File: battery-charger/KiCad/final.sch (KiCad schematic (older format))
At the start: 19 parts, among them Q1 MOSFET_P, SW1 SPST, U1 BQ2057W

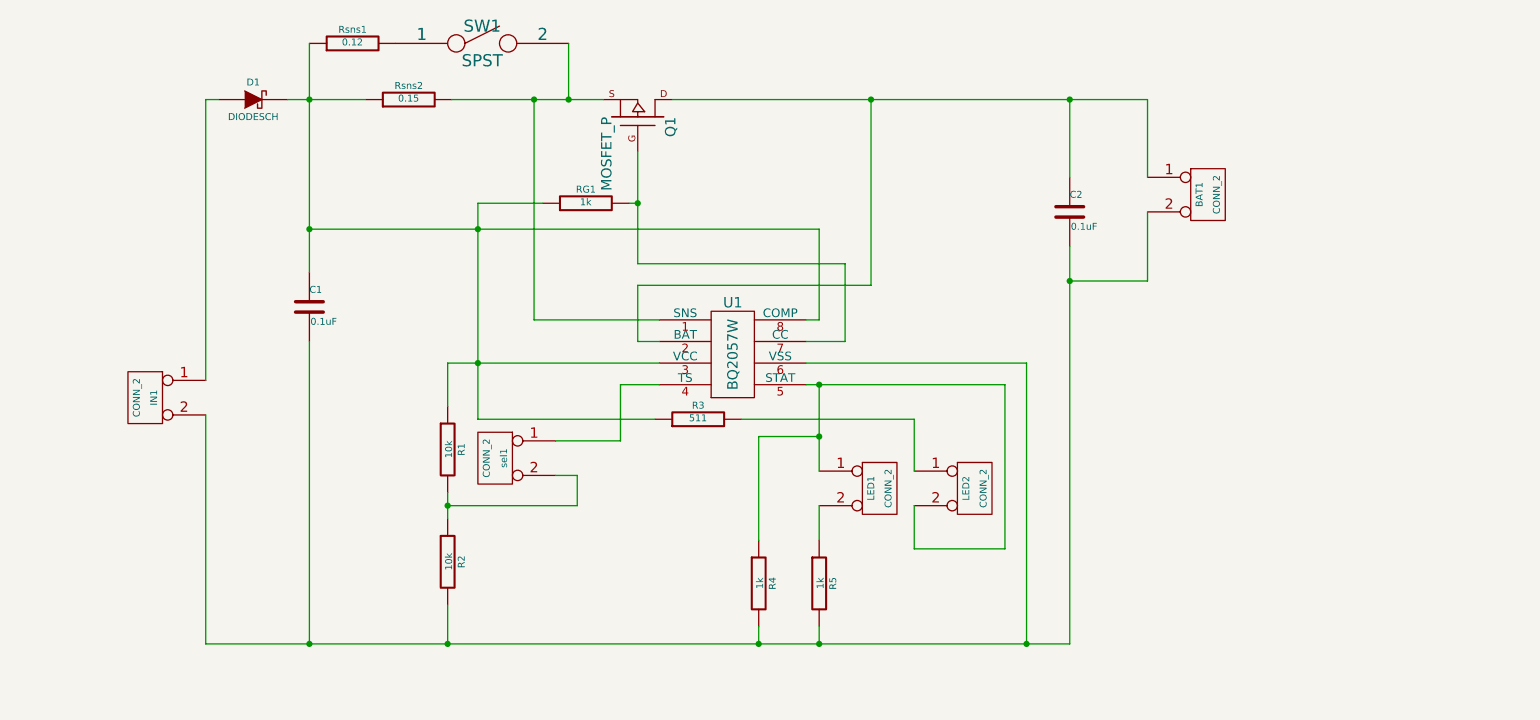
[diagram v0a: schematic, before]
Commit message: Link correctly the specific footprint library and change one component
The two connectors are repleaced by a 3-pin connector in order to reduce
length of power traces.
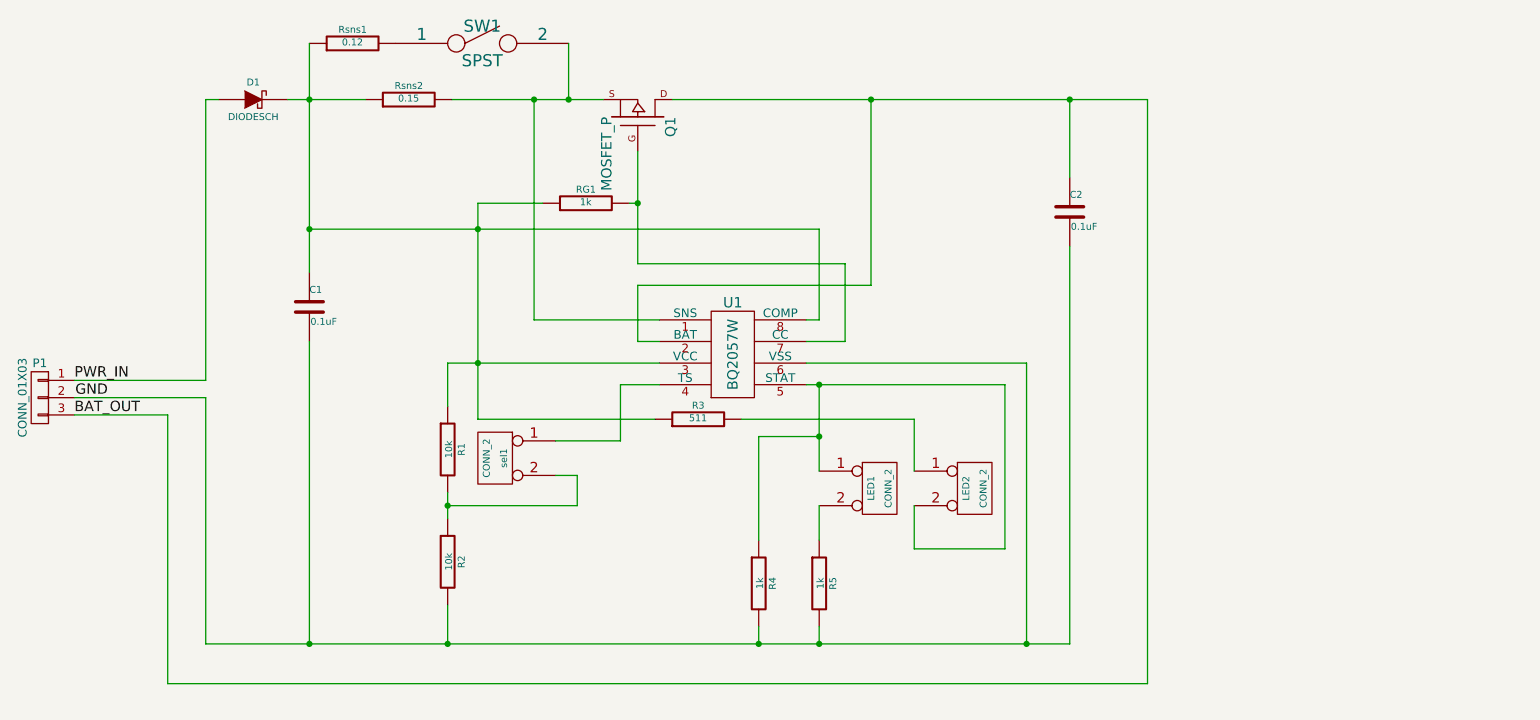
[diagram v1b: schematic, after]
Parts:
- removed BAT1, IN1: CONN_2, symbol CONN_2
- added P1: CONN_01X03, symbol CONN_01X03
- U1: footprint ~ -> (none)
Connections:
- net BAT_OUT: now reaches C2.1, Q1.D, U1.2 (BAT)
- net BAT_OUT: now also P1.3 (P3)
- net GND: now reaches C1.2, C2.2, R2.2, R4.2, R5.2, U1.6 (VSS)
- net GND: now also P1.2 (P2)
- net PWR_IN: now reaches D1.1 (A)
- net PWR_IN: now also P1.1 (P1)
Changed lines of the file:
@@
 EESchema Schematic File Version 2
-LIBS:final-rescue
 LIBS:power
 LIBS:device
@@
 LIBS:contrib
 LIBS:valves
+LIBS:special
 LIBS:final-cache
 EELAYER 25 0
@@
 	1    0    0    -1
 $EndComp
-Connection ~ 4850 2400
-Wire Wire Line
-	3550 3150 6500 3150
-Wire Wire Line
-	5650 2400 8400 2400
-Wire Wire Line
-	7950 2850 7950 2400
-Connection ~ 7950 2400
-Connection ~ 6800 2400
-Wire Wire Line
-	6500 4750 6500 4950
-Wire Wire Line
-	6500 5550 6500 5450
-Connection ~ 6500 5550
-Wire Wire Line
-	6150 5550 6150 5450
-Connection ~ 6150 5550
-Wire Wire Line
-	7950 5550 2950 5550
-Wire Wire Line
-	6500 4050 6500 4550
-Wire Wire Line
-	6150 4350 6500 4350
-Wire Wire Line
-	6150 4350 6150 4950
-Wire Wire Line
-	6050 4250 7050 4250
 $Comp
 L DIODESCH D1
@@
 	1    0    0    -1
 $EndComp
-Wire Wire Line
-	7950 3250 7950 5550
-Wire Wire Line
-	7950 3450 8400 3450
-$Comp
-L CONN_2 IN1
-U 1 1 551BBEB1
-P 2600 4125
-F 0 "IN1" V 2550 4125 40  0000 C CNN
-F 1 "CONN_2" V 2650 4125 40  0000 C CNN
-F 2 "" H 2600 4125 60  0000 C CNN
-F 3 "" H 2600 4125 60  0000 C CNN
-	1    2600 4125
-	-1   0    0    -1
-$EndComp
-$Comp
-L CONN_2 BAT1
-U 1 1 551BBF37
-P 8750 2950
-F 0 "BAT1" V 8700 2950 40  0000 C CNN
-F 1 "CONN_2" V 8800 2950 40  0000 C CNN
-F 2 "" H 8750 2950 60  0000 C CNN
-F 3 "" H 8750 2950 60  0000 C CNN
-	1    8750 2950
-	1    0    0    -1
-$EndComp
-Wire Wire Line
-	8400 2400 8400 2850
-Wire Wire Line
-	8400 3450 8400 3050
 $Comp
 L CONN_2 LED1
@@
 	1    0    0    -1
 $EndComp
-Wire Wire Line
-	7050 4250 7050 4550
-Wire Wire Line
-	7050 4750 7050 5000
-Wire Wire Line
-	7050 5000 7575 5000
-Wire Wire Line
-	7575 5000 7575 4050
-Wire Wire Line
-	7575 4050 6425 4050
-Wire Wire Line
-	6425 3800 6650 3800
-Wire Wire Line
-	6650 3800 6650 3350
-Wire Wire Line
-	6650 3350 5450 3350
-Wire Wire Line
-	5450 3350 5450 2700
-Wire Wire Line
-	5400 3000 5450 3000
-Connection ~ 5450 3000
-Wire Wire Line
-	6425 3675 6500 3675
-Wire Wire Line
-	6500 3675 6500 3150
-Wire Wire Line
-	6425 3925 7700 3925
-Wire Wire Line
-	7700 3925 7700 5550
-Wire Wire Line
-	4350 3925 5575 3925
-Wire Wire Line
-	5575 3675 4850 3675
-Wire Wire Line
-	4850 3675 4850 2400
-Wire Wire Line
-	5575 3800 5450 3800
-Wire Wire Line
-	5450 3800 5450 3475
-Wire Wire Line
-	5450 3475 6800 3475
-Wire Wire Line
-	6800 3475 6800 2400
-Wire Wire Line
-	4900 3000 4525 3000
-Wire Wire Line
-	4525 3000 4525 4250
-Connection ~ 4525 3150
-Connection ~ 7700 5550
-Connection ~ 7950 3450
-Wire Wire Line
-	5350 4050 5575 4050
-Connection ~ 6500 4050
-Connection ~ 6500 4350
-Wire Wire Line
-	4525 4250 5550 4250
-Connection ~ 4525 3925
 $Comp
 L CONN_2 sel1
@@
 	-1   0    0    -1
 $EndComp
-Wire Wire Line
-	5350 4375 4975 4375
-Wire Wire Line
-	5350 4050 5350 4375
 $Comp
 L R-RESCUE-final R1
@@
 	1    0    0    -1
 $EndComp
-Wire Wire Line
-	4350 4175 4350 3925
-Wire Wire Line
-	4350 4675 4350 4825
-Wire Wire Line
-	4350 5550 4350 5325
-Connection ~ 4350 5550
-Wire Wire Line
-	4975 4575 5100 4575
-Wire Wire Line
-	5100 4575 5100 4750
-Wire Wire Line
-	5100 4750 4350 4750
-Connection ~ 4350 4750
 $Comp
 L R-RESCUE-final Rsns1
@@
 	1    0    0    -1
 $EndComp
-Wire Wire Line
-	2950 5550 2950 4225
-Wire Wire Line
-	2950 4025 2950 2400
+$Comp
+L CONN_01X03 P1
+U 1 1 5A0DA7EC
+P 1990 4125
+F 0 "P1" H 1990 4325 50  0000 C CNN
+F 1 "CONN_01X03" V 2090 4125 50  0000 C CNN
+F 2 "" H 1990 4125 60  0000 C CNN
+F 3 "" H 1990 4125 60  0000 C CNN
+	1    1990 4125
+	-1   0    0    -1
+$EndComp
+Connection ~ 4850 2400
+Wire Wire Line
+	3550 3150 6500 3150
+Wire Wire Line
+	5650 2400 8400 2400
+Wire Wire Line
+	7950 2850 7950 2400
+Connection ~ 7950 2400
+Connection ~ 6800 2400
+Wire Wire Line
+	6500 4750 6500 4950
+Wire Wire Line
+	6500 5550 6500 5450
+Connection ~ 6500 5550
+Wire Wire Line
+	6150 5550 6150 5450
+Connection ~ 6150 5550
+Wire Wire Line
+	6500 4050 6500 4550
+Wire Wire Line
+	6150 4350 6500 4350
+Wire Wire Line
+	6150 4350 6150 4950
+Wire Wire Line
+	6050 4250 7050 4250
+Wire Wire Line
+	7950 5550 7950 3250
+Wire Wire Line
+	8400 2400 8400 5780
+Wire Wire Line
+	7050 4250 7050 4550
+Wire Wire Line
+	7050 4750 7050 5000
+Wire Wire Line
+	7050 5000 7575 5000
+Wire Wire Line
+	7575 5000 7575 4050
+Wire Wire Line
+	7575 4050 6425 4050
+Wire Wire Line
+	6425 3800 6650 3800
+Wire Wire Line
+	6650 3800 6650 3350
+Wire Wire Line
+	6650 3350 5450 3350
+Wire Wire Line
+	5450 3350 5450 2700
+Wire Wire Line
+	5400 3000 5450 3000
+Connection ~ 5450 3000
+Wire Wire Line
+	6425 3675 6500 3675
+Wire Wire Line
+	6500 3675 6500 3150
+Wire Wire Line
+	6425 3925 7700 3925
+Wire Wire Line
+	7700 3925 7700 5550
+Wire Wire Line
+	4350 3925 5575 3925
+Wire Wire Line
+	5575 3675 4850 3675
+Wire Wire Line
+	4850 3675 4850 2400
+Wire Wire Line
+	5575 3800 5450 3800
+Wire Wire Line
+	5450 3800 5450 3475
+Wire Wire Line
+	5450 3475 6800 3475
+Wire Wire Line
+	6800 3475 6800 2400
+Wire Wire Line
+	4900 3000 4525 3000
+Wire Wire Line
+	4525 3000 4525 4250
+Connection ~ 4525 3150
+Connection ~ 7700 5550
+Wire Wire Line
+	5350 4050 5575 4050
+Connection ~ 6500 4050
+Connection ~ 6500 4350
+Wire Wire Line
+	4525 4250 5550 4250
+Connection ~ 4525 3925
+Wire Wire Line
+	5350 4375 4975 4375
+Wire Wire Line
+	5350 4050 5350 4375
+Wire Wire Line
+	4350 4175 4350 3925
+Wire Wire Line
+	4350 4675 4350 4825
+Wire Wire Line
+	4350 5550 4350 5325
+Connection ~ 4350 5550
+Wire Wire Line
+	4975 4575 5100 4575
+Wire Wire Line
+	5100 4575 5100 4750
+Wire Wire Line
+	5100 4750 4350 4750
+Connection ~ 4350 4750
 Wire Wire Line
 	2950 2400 3025 2400
@@
 	5050 2075 5050 2400
 Connection ~ 5050 2400
+Wire Wire Line
+	2950 5550 7950 5550
+Wire Wire Line
+	2950 5550 2950 4125
+Wire Wire Line
+	2190 4025 2950 4025
+Wire Wire Line
+	2950 4025 2950 2400
+Wire Wire Line
+	2950 4125 2190 4125
+Wire Wire Line
+	8400 5780 2730 5780
+Wire Wire Line
+	2730 5780 2730 4225
+Wire Wire Line
+	2730 4225 2190 4225
+Text Label 2190 4025 0    60   ~ 0
+PWR_IN
+Text Label 2195 4125 0    60   ~ 0
+GND
+Text Label 2190 4225 0    60   ~ 0
+BAT_OUT
 $Comp
 L BQ2057W U1
-U 1 1 555B9281
+U 1 1 5A0DCE03
 P 5875 4125
 F 0 "U1" H 6000 4675 60  0000 C CNN
 F 1 "BQ2057W" V 6000 4375 60  0000 C CNN
-F 2 "~" H 5625 4525 60  0000 C CNN
-F 3 "~" H 5625 4525 60  0000 C CNN
+F 2 "" H 5625 4525 60  0000 C CNN
+F 3 "" H 5625 4525 60  0000 C CNN
 	1    5875 4125
 	1    0    0    -1

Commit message: Update the v2.0 of the battery charger PCB
Include the Bill of Materials (BOM) with all the components

Include all the footprints in the footprint library
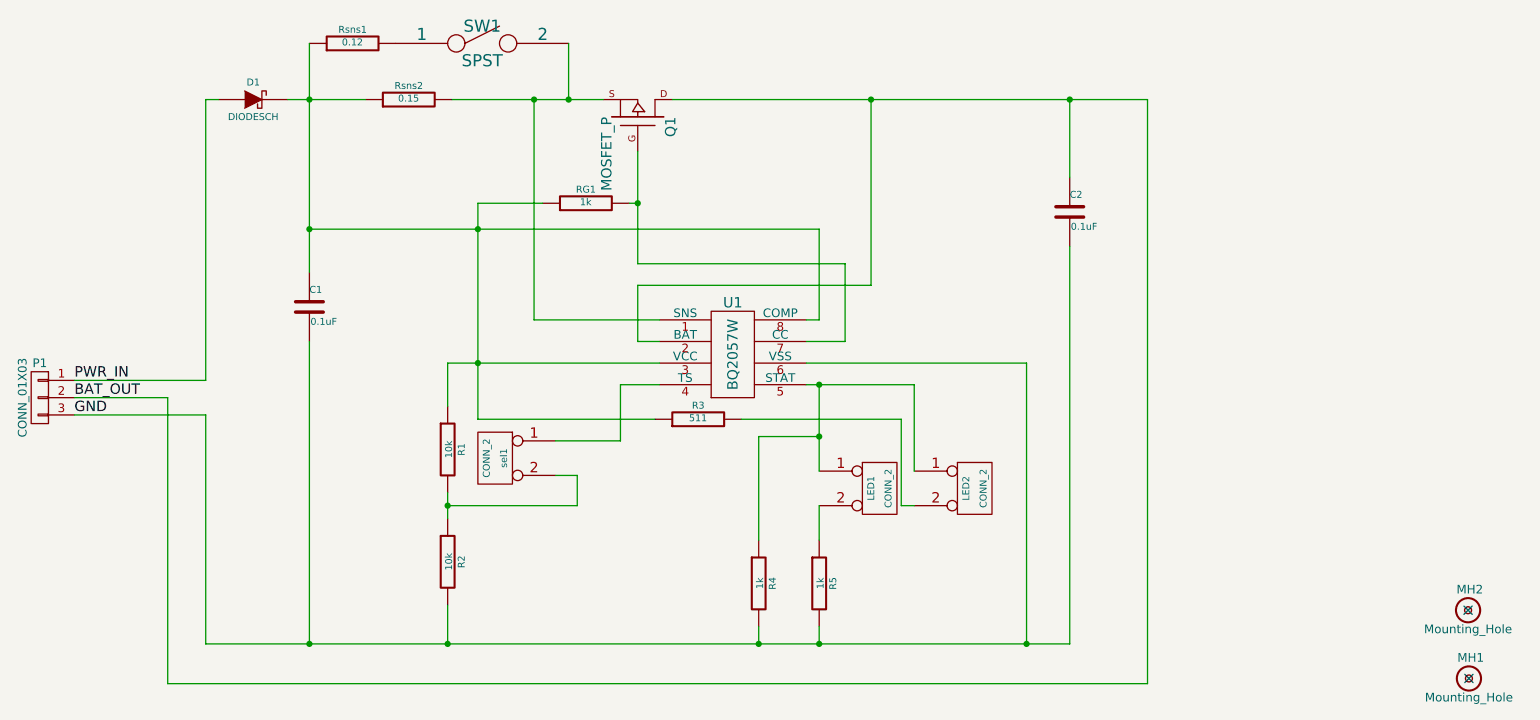
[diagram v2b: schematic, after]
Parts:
- added MH1, MH2: Mounting_Hole, footprint:Mounting_hole, symbol Mounting_Hole
- C1, C2: footprint ~ -> footprint:C_0603
- D1: footprint ~ -> footprint:D_DO-201AD
- LED1, LED2: footprint (none) -> footprint:Molex_02x01
- P1: footprint (none) -> footprint:Molex_03x01_Straight
- Q1: footprint ~ -> footprint:TO-220-3
- R1, R2, R3: footprint ~ -> footprint:R_THT_0.54
- R4, R5, RG1: footprint ~ -> footprint:R_THT_0.78
- Rsns1, Rsns2: footprint ~ -> footprint:R_2512_HandSoldering
- SW1: footprint ~ -> footprint:Switch
- U1: footprint (none) -> footprint:SOIC-8_Handsoldering
- sel1: footprint (none) -> footprint:Pin_Header_Straight_01x02
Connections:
- net BAT_OUT: now also P1.2 (P2); no longer P1.3 (P3)
- net GND: now also P1.3 (P3); no longer P1.2 (P2)
- net at R3.2: now also LED2.2 (PM); no longer LED2.1 (P1)
- net at LED1.1 (P1), R4.1, U1.5 (STAT): now also LED2.1 (P1); no longer LED2.2 (PM)
- no-connect marks 0 -> 2
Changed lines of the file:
@@
 F 0 "Rsns2" V 4205 2400 40  0000 C CNN
 F 1 "0.15" V 4132 2401 40  0000 C CNN
-F 2 "~" V 4055 2400 30  0000 C CNN
+F 2 "footprint:R_2512_HandSoldering" V 4055 2400 30  0001 C CNN
 F 3 "~" H 4125 2400 30  0000 C CNN
 	1    4125 2400
@@
 F 0 "Q1" H 5450 2690 60  0000 R CNN
 F 1 "MOSFET_P" H 5450 2320 60  0000 R CNN
-F 2 "~" H 5450 2500 60  0000 C CNN
+F 2 "footprint:TO-220-3" H 5450 2500 60  0001 C CNN
 F 3 "~" H 5450 2500 60  0000 C CNN
 	1    5450 2500
@@
 F 0 "R3" V 5880 4250 40  0000 C CNN
 F 1 "511" V 5807 4251 40  0000 C CNN
-F 2 "~" V 5730 4250 30  0000 C CNN
+F 2 "footprint:R_THT_0.54" V 5730 4250 30  0001 C CNN
 F 3 "~" H 5800 4250 30  0000 C CNN
 	1    5800 4250
@@
 F 0 "C2" H 7950 3150 40  0000 L CNN
 F 1 "0.1uF" H 7956 2965 40  0000 L CNN
-F 2 "~" H 7988 2900 30  0000 C CNN
+F 2 "footprint:C_0603" H 7988 2900 30  0001 C CNN
 F 3 "~" H 7950 3050 60  0000 C CNN
 	1    7950 3050
@@
 F 0 "C1" H 3550 3700 40  0000 L CNN
 F 1 "0.1uF" H 3556 3515 40  0000 L CNN
-F 2 "~" H 3588 3450 30  0000 C CNN
+F 2 "footprint:C_0603" H 3588 3450 30  0001 C CNN
 F 3 "~" H 3550 3600 60  0000 C CNN
 	1    3550 3600
@@
 F 0 "RG1" V 5230 3000 40  0000 C CNN
 F 1 "1k" V 5157 3001 40  0000 C CNN
-F 2 "~" V 5080 3000 30  0000 C CNN
+F 2 "footprint:R_THT_0.78" V 5080 3000 30  0001 C CNN
 F 3 "~" H 5150 3000 30  0000 C CNN
 	1    5150 3000
@@
 F 0 "R5" V 6580 5200 40  0000 C CNN
 F 1 "1k" V 6507 5201 40  0000 C CNN
-F 2 "~" V 6430 5200 30  0000 C CNN
+F 2 "footprint:R_THT_0.78" V 6430 5200 30  0001 C CNN
 F 3 "~" H 6500 5200 30  0000 C CNN
 	1    6500 5200
@@
 F 0 "R4" V 6230 5200 40  0000 C CNN
 F 1 "1k" V 6157 5201 40  0000 C CNN
-F 2 "~" V 6080 5200 30  0000 C CNN
+F 2 "footprint:R_THT_0.78" V 6080 5200 30  0001 C CNN
 F 3 "~" H 6150 5200 30  0000 C CNN
 	1    6150 5200
@@
 F 0 "D1" H 3225 2500 40  0000 C CNN
 F 1 "DIODESCH" H 3225 2300 40  0000 C CNN
-F 2 "~" H 3225 2400 60  0000 C CNN
+F 2 "footprint:D_DO-201AD" H 3225 2400 60  0001 C CNN
 F 3 "~" H 3225 2400 60  0000 C CNN
 	1    3225 2400
@@
 F 0 "LED1" V 6800 4650 40  0000 C CNN
 F 1 "CONN_2" V 6900 4650 40  0000 C CNN
-F 2 "" H 6850 4650 60  0000 C CNN
+F 2 "footprint:Molex_02x01" H 6850 4650 60  0001 C CNN
 F 3 "" H 6850 4650 60  0000 C CNN
 	1    6850 4650
@@
 F 0 "LED2" V 7350 4650 40  0000 C CNN
 F 1 "CONN_2" V 7450 4650 40  0000 C CNN
-F 2 "" H 7400 4650 60  0000 C CNN
+F 2 "footprint:Molex_02x01" H 7400 4650 60  0001 C CNN
 F 3 "" H 7400 4650 60  0000 C CNN
 	1    7400 4650
@@
 F 0 "sel1" V 4575 4475 40  0000 C CNN
 F 1 "CONN_2" V 4675 4475 40  0000 C CNN
-F 2 "" H 4625 4475 60  0000 C CNN
+F 2 "footprint:Pin_Header_Straight_01x02" H 4625 4475 60  0001 C CNN
 F 3 "" H 4625 4475 60  0000 C CNN
 	1    4625 4475
@@
 F 0 "R1" V 4430 4425 40  0000 C CNN
 F 1 "10k" V 4357 4426 40  0000 C CNN
-F 2 "~" V 4280 4425 30  0000 C CNN
+F 2 "footprint:R_THT_0.54" V 4280 4425 30  0001 C CNN
 F 3 "~" H 4350 4425 30  0000 C CNN
 	1    4350 4425
@@
 F 0 "R2" V 4430 5075 40  0000 C CNN
 F 1 "10k" V 4357 5076 40  0000 C CNN
-F 2 "~" V 4280 5075 30  0000 C CNN
+F 2 "footprint:R_THT_0.54" V 4280 5075 30  0001 C CNN
 F 3 "~" H 4350 5075 30  0000 C CNN
 	1    4350 5075
@@
 F 0 "Rsns1" V 3880 2075 40  0000 C CNN
 F 1 "0.12" V 3807 2076 40  0000 C CNN
-F 2 "~" V 3730 2075 30  0000 C CNN
+F 2 "footprint:R_2512_HandSoldering" V 3730 2075 30  0001 C CNN
 F 3 "~" H 3800 2075 30  0000 C CNN
 	1    3800 2075
@@
 F 0 "SW1" H 4550 2175 70  0000 C CNN
 F 1 "SPST" H 4550 1975 70  0000 C CNN
-F 2 "~" H 4550 2075 60  0000 C CNN
+F 2 "footprint:Switch" H 4550 2310 60  0001 C CNN
 F 3 "~" H 4550 2075 60  0000 C CNN
 	1    4550 2075
@@
 F 0 "P1" H 1990 4325 50  0000 C CNN
 F 1 "CONN_01X03" V 2090 4125 50  0000 C CNN
-F 2 "" H 1990 4125 60  0000 C CNN
+F 2 "footprint:Molex_03x01_Straight" H 1990 4125 60  0001 C CNN
 F 3 "" H 1990 4125 60  0000 C CNN
 	1    1990 4125
@@
 	6150 4350 6150 4950
 Wire Wire Line
-	6050 4250 7050 4250
-Wire Wire Line
 	7950 5550 7950 3250
 Wire Wire Line
 	8400 2400 8400 5780
 Wire Wire Line
-	7050 4250 7050 4550
-Wire Wire Line
-	7050 4750 7050 5000
-Wire Wire Line
-	7050 5000 7575 5000
-Wire Wire Line
-	7575 5000 7575 4050
-Wire Wire Line
-	7575 4050 6425 4050
+	6425 4050 7050 4050
 Wire Wire Line
 	6425 3800 6650 3800
@@
 	2950 5550 7950 5550
 Wire Wire Line
-	2950 5550 2950 4125
-Wire Wire Line
 	2190 4025 2950 4025
 Wire Wire Line
 	2950 4025 2950 2400
 Wire Wire Line
-	2950 4125 2190 4125
-Wire Wire Line
 	8400 5780 2730 5780
-Wire Wire Line
-	2730 5780 2730 4225
-Wire Wire Line
-	2730 4225 2190 4225
 Text Label 2190 4025 0    60   ~ 0
 PWR_IN
-Text Label 2195 4125 0    60   ~ 0
+Text Label 2190 4225 0    60   ~ 0
 GND
-Text Label 2190 4225 0    60   ~ 0
+Text Label 2190 4125 0    60   ~ 0
 BAT_OUT
 $Comp
@@
 F 0 "U1" H 6000 4675 60  0000 C CNN
 F 1 "BQ2057W" V 6000 4375 60  0000 C CNN
-F 2 "" H 5625 4525 60  0000 C CNN
+F 2 "footprint:SOIC-8_Handsoldering" H 5625 4525 60  0001 C CNN
 F 3 "" H 5625 4525 60  0000 C CNN
 	1    5875 4125
 	1    0    0    -1
 $EndComp
+Wire Wire Line
+	2950 5550 2950 4225
+Wire Wire Line
+	2950 4225 2190 4225
+Wire Wire Line
+	2730 5780 2730 4125
+Wire Wire Line
+	2730 4125 2190 4125
+Wire Wire Line
+	6050 4250 6975 4250
+Wire Wire Line
+	6975 4250 6975 4750
+Wire Wire Line
+	6975 4750 7050 4750
+Wire Wire Line
+	7050 4050 7050 4550
+$Comp
+L Mounting_Hole MH1
+U 1 1 5A12AA51
+P 10260 5750
+F 0 "MH1" H 10270 5870 50  0000 C CNN
+F 1 "Mounting_Hole" H 10260 5640 50  0000 C CNN
+F 2 "footprint:Mounting_hole" H 10260 5750 60  0001 C CNN
+F 3 "" H 10260 5750 60  0000 C CNN
+	1    10260 5750
+	1    0    0    -1
+$EndComp
+$Comp
+L Mounting_Hole MH2
+U 1 1 5A12AD46
+P 10255 5355
+F 0 "MH2" H 10265 5475 50  0000 C CNN
+F 1 "Mounting_Hole" H 10255 5245 50  0000 C CNN
+F 2 "footprint:Mounting_hole" H 10255 5355 60  0001 C CNN
+F 3 "" H 10255 5355 60  0000 C CNN
+	1    10255 5355
+	1    0    0    -1
+$EndComp
+NoConn ~ 10260 5750
+NoConn ~ 10255 5355
 $EndSCHEMATC
